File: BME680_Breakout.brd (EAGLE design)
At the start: 160 x 100 mm, 23 parts, among them U1 BME680, U4 PCA9515ADP, U8 LD1117XX

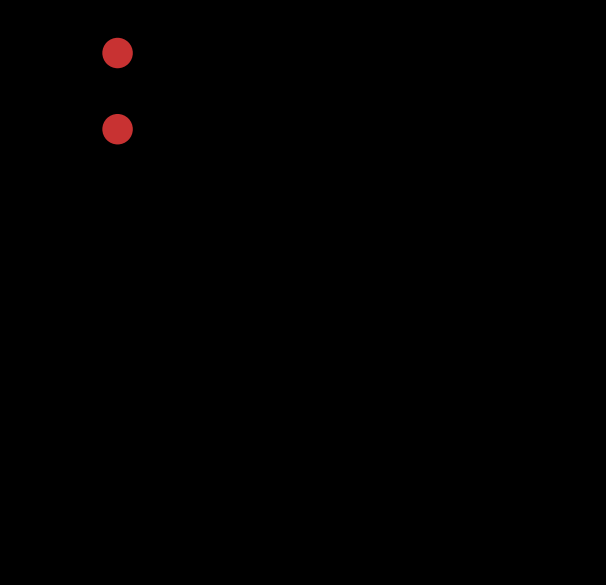
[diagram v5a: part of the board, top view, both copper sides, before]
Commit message: asded zener diode and ptc fuse to address select input
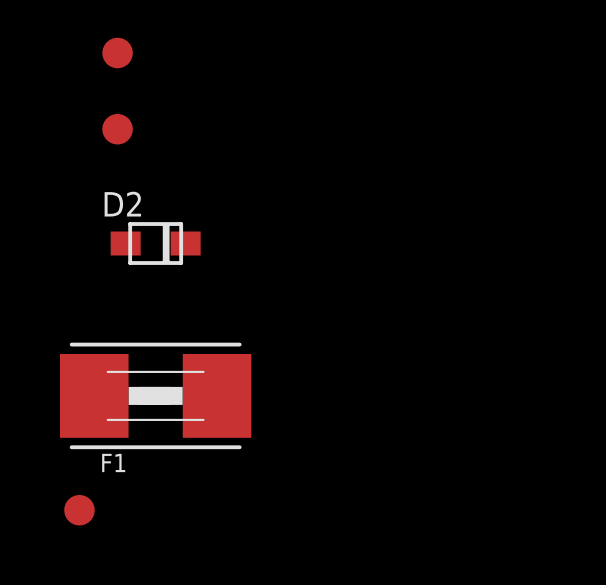
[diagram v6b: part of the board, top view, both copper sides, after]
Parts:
- added D2: DDZ3V3BSF-7, adafruit:SOD-323F
- added F1: (no value), adafruit:1812
- added TP4: TEST-POINT3X4, SparkFun-Passives:PAD.03X.04
- D1: value (none) -> 1N4148
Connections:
- new net ADDR_SELECT_VCCIO: F1.2, JP1.7
- net ADDR_SELECT_3V3: now also D2.C, F1.1, TP4.P$1; no longer JP1.7
- net GND: now also D2.A
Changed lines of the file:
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@@
 <element name="SJ2" library="SparkFun-Passives" package="PAD-JUMPER-2-NO_YES_SILK" value="JUMPER-PAD-2-NOYES_SILK" x="-49.53" y="-25.4"/>
 <element name="R6" library="SparkFun-Passives" package="0805" value="10k" x="-53.34" y="-25.4"/>
-<element name="D1" library="adafruit" package="SOD-323F" value="" x="-52.07" y="-30.48"/>
+<element name="D1" library="adafruit" package="SOD-323F" value="1N4148" x="-52.07" y="-30.48"/>
 <element name="R3" library="SparkFun-Passives" package="0805" value="10k" x="-57.15" y="-29.21"/>
 <element name="U8" library="wicked-device" package="DPAK" value="LD1117XX" x="-53.34" y="-39.37"/>
@@
 <element name="TP2" library="SparkFun-Passives" package="PAD.03X.04" value="TEST-POINT3X4" x="-68.58" y="-48.26"/>
 <element name="TP3" library="SparkFun-Passives" package="PAD.03X.04" value="TEST-POINT3X4" x="-68.58" y="-50.8"/>
+<element name="D2" library="adafruit" package="SOD-323F" value="DDZ3V3BSF-7" x="-67.31" y="-54.61"/>
+<element name="F1" library="adafruit" package="1812" value="" x="-67.31" y="-59.69"/>
+<element name="TP4" library="SparkFun-Passives" package="PAD.03X.04" value="TEST-POINT3X4" x="-69.85" y="-63.5"/>
 </elements>
 <signals>
@@
 <contactref element="C5" pad="2"/>
 <contactref element="R7" pad="2"/>
+<contactref element="D2" pad="A"/>
+<wire x1="-67.68" y1="-41.91" x2="-68.31" y2="-54.61" width="0" layer="19" extent="1-1"/>
 <wire x1="-63.87" y1="-41.91" x2="-67.68" y2="-41.91" width="0" layer="19" extent="1-1"/>
 <wire x1="-60.06" y1="-41.91" x2="-63.87" y2="-41.91" width="0" layer="19" extent="1-1"/>
@@
 <contactref element="SJ2" pad="2"/>
 <contactref element="R3" pad="2"/>
-<contactref element="JP1" pad="7"/>
+<contactref element="F1" pad="1"/>
+<contactref element="D2" pad="C"/>
+<contactref element="TP4" pad="P$1"/>
+<wire x1="-69.356" y1="-59.69" x2="-69.85" y2="-63.5" width="0" layer="19" extent="1-1"/>
+<wire x1="-66.31" y1="-54.61" x2="-69.356" y2="-59.69" width="0" layer="19" extent="1-1"/>
+<wire x1="-56.25" y1="-29.21" x2="-66.31" y2="-54.61" width="0" layer="19" extent="1-1"/>
 <wire x1="-49.08" y1="-25.4" x2="-56.25" y2="-29.21" width="0" layer="19" extent="1-1"/>
-<wire x1="-29.21" y1="-20.32" x2="-49.08" y2="-25.4" width="0" layer="19" extent="1-1"/>
-<wire x1="-16.5275" y1="2.61" x2="-29.21" y2="-20.32" width="0" layer="19" extent="1-1"/>
+<wire x1="-16.5275" y1="2.61" x2="-49.08" y2="-25.4" width="0" layer="19" extent="1-1"/>
 </signal>
 <signal name="SLAVE_SCL_3V3">
@@
 <wire x1="-31.75" y1="-20.32" x2="-51.07" y2="-30.48" width="0" layer="19" extent="1-1"/>
 </signal>
+<signal name="ADDR_SELECT_VCCIO">
+<contactref element="JP1" pad="7"/>
+<contactref element="F1" pad="2"/>
+<wire x1="-29.21" y1="-20.32" x2="-65.264" y2="-59.69" width="0" layer="19" extent="1-1"/>
+</signal>
 </signals>

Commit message: initial routing of PCB
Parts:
- added SJ1: JUMPER-PAD-2-NC_BY_TRACE, SparkFun-Passives:PAD-JUMPER-2-NC_BY_TRACE_YES_SILK
- added SJ3: SOLDERJUMPERNC2, SparkFun-Retired:SJ_2S-NOTRACE
- added STANDOFF1, STANDOFF2, STANDOFF3, STANDOFF4: STAND-OFF, SparkFun-Electromechanical:STAND-OFF
- added U$1: (no value), wicked-device:WICKEDLOGOTYPE2
- added U$2: (no value), wicked-device:WICKEDLOGOTYPE
- moved TP2 109.5 mm to (23.4, 11.2)
- moved R7 107.1 mm to (21.8, 15.5), turned to 270 degrees
- moved C5 106.8 mm to (28.7, 9.65), turned to 270 degrees
- moved TP1 106.6 mm to (23.4, 8.13)
- moved C4 104.5 mm to (31.8, 6.35), turned to 180 degrees
- moved TP4 103.3 mm to (7.62, 4.83)
- moved F1 102.6 mm to (10.2, 7.62)
- moved TP3 102.0 mm to (11.7, 12.2)
- moved U8 101.2 mm to (33.8, 12.2)
- moved D2 99.3 mm to (7.11, 11.2)
- moved R3 82.6 mm to (13.0, 14.5), turned to 180 degrees
- moved R6 77.7 mm to (15.2, 11.2), turned to 270 degrees
- moved D1 77.3 mm to (15.2, 7.62), turned to 270 degrees
- moved SJ5 66.0 mm to (17.3, 6.86), turned to 180 degrees
- moved SJ4 65.7 mm to (20.8, 6.86)
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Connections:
- net SJ_MASTER_SCL_3V3 renamed SJ_MASTER_SCL_VIO
- net SJ_MASTER_SDA_3V3 renamed SJ_MASTER_SDA_VIO
- removed net MASTER_SCL_3V3: SJ5.1
- removed net MASTER_SDA_3V3: SJ4.1
- new net N$1: SJ1.2, U8.4
- net 3.3V: now also SJ1.1, SJ3.2; no longer U8.4
- net MASTER_SCL_VIO: now also JP1.5, SJ5.1; no longer JP1.3
- net MASTER_SDA_VIO: now also SJ4.1
- net SLAVE_I2C_ENABLE: now also JP1.3; no longer JP1.5
- net VCCIO: now also SJ3.1
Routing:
- net 3.3V: track 0.00 -> 71.1 mm, vias 0 -> 4
- net ADDR_SELECT_3V3: track 0.00 -> 32.9 mm
- net GND: track 0.00 -> 27.2 mm, vias 0 -> 9
- net VCCIO: track 0.00 -> 25.1 mm
- net CSB_3V3: track 0.00 -> 23.1 mm
- net SLAVE_I2C_ENABLE: track 0.00 -> 23.1 mm, vias 0 -> 2
- net SJ_MASTER_SCL_VIO: track 0.00 -> 11.3 mm, vias 0 -> 2
- net MASTER_SDA_VIO: track 0.00 -> 10.9 mm
- net MASTER_SCL_VIO: track 0.00 -> 10.9 mm
- net N$1: track 0.00 -> 6.77 mm
- net SLAVE_SDA_3V3: track 0.00 -> 6.47 mm
- net ADDR_SELECT_VCCIO: track 0.00 -> 5.79 mm
- net CSB_VIO: track 0.00 -> 4.59 mm
- net SLAVE_SCL_3V3: track 0.00 -> 3.98 mm
- net SJ_MASTER_SDA_VIO: track 0.00 -> 3.66 mm
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- added copper zone on layer 16, net GND
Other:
- board size 160 x 100 mm -> 38.1 x 25.4 mm
- board text added: "*"
- board text added: "3V"
- board text added: "AD"
- board text added: "CK"
- board text added: "CS"
- board text added: "DT"
- board text added: "EN"
- board text added: "GD"
- board text added: "VI"

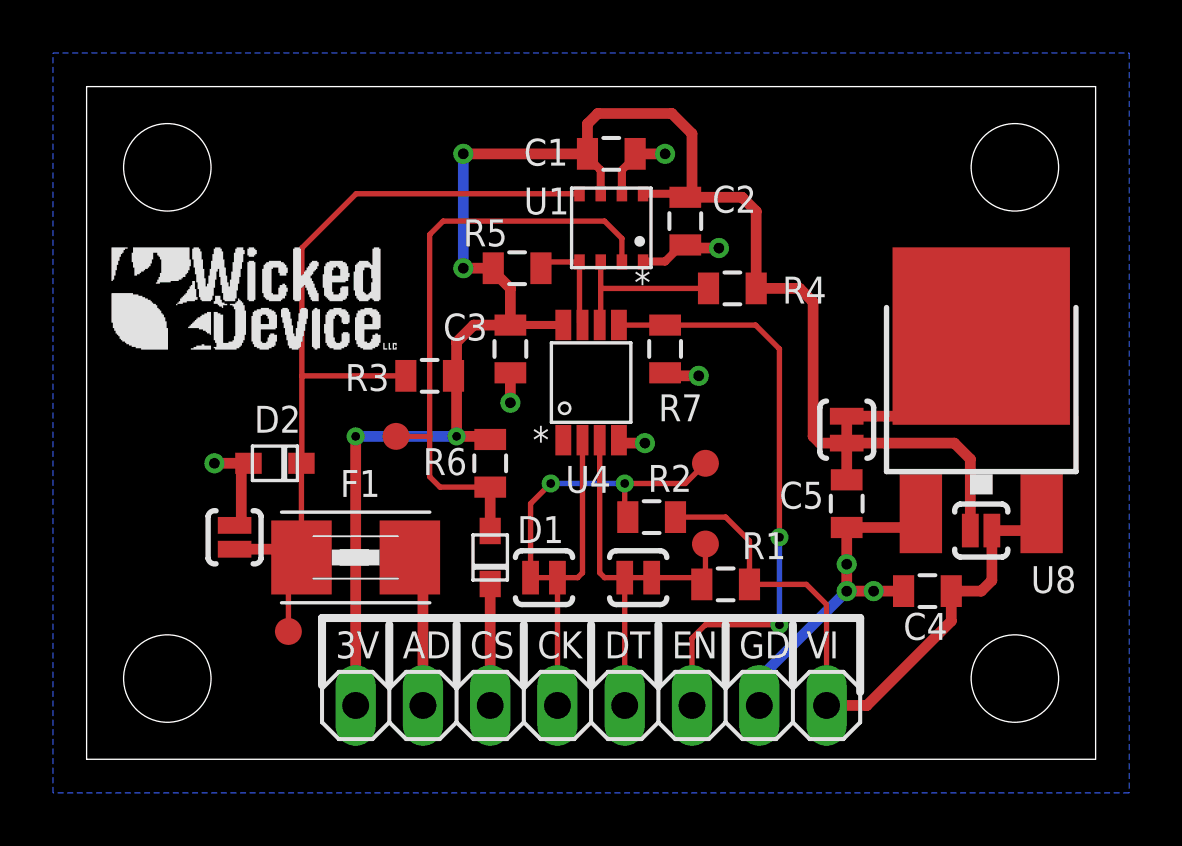
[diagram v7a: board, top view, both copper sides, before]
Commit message: added silk screen to back side; added to solder jumpers; minor routing changes
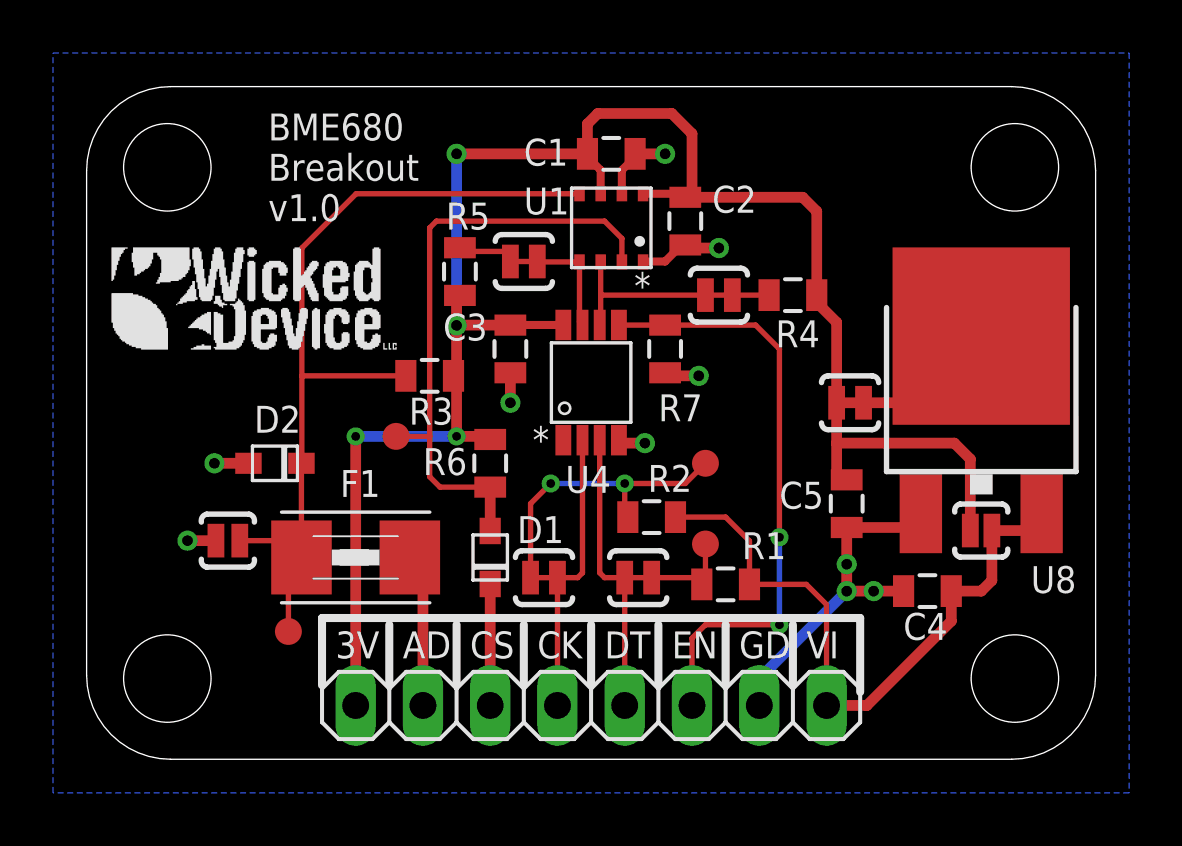
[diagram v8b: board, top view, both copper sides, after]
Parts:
- removed U$2: (no value), wicked-device:WICKEDLOGOTYPE
- added SJ6, SJ7: JUMPER-PAD-2-NC_BY_TRACE, SparkFun-Passives:PAD-JUMPER-2-NC_BY_TRACE_YES_SILK
- moved R4 2.30 mm to (26.7, 17.5)
- moved R5 2.16 mm to (14.1, 18.4), turned to 90 degrees
- moved SJ1 1.02 mm to (28.8, 13.5), turned to 0 degrees
- moved SJ2 0.28 mm to (5.33, 8.26), turned to 0 degrees
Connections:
- new net N$3: R4.2, SJ6.2
- new net N$4: R5.2, SJ7.2
- net SLAVE_SCL_3V3: now also SJ7.1; no longer R5.2
- net SLAVE_SDA_3V3: now also SJ6.1; no longer R4.2
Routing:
- net N$4: track 0.00 -> 2.34 mm
- net GND: track 27.2 -> 25.8 mm, vias 9 -> 10
- net N$3: track 0.00 -> 1.39 mm
- net 3.3V: track 71.1 -> 72.4 mm
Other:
- outline, holes or cut-outs redrawn
- board text added: "3V = 3.3V REG OUT / 3.3V INPUT"
- board text added: "ADDR = AD"
- board text added: "BME680 Breakout v1.0"
- board text added: "FOR I2C BUS ISOLATION"
- board text added: "GD = GROUND"
- board text added: "I2C"
- board text added: "MISO = AD"
- board text added: "MOSI = DT"
- board text added: "NCS = CS"
- board text added: "SCK = CK"
- board text added: "SCL = CK"
- board text added: "SDA = DT"
- board text added: "SELECT = EN"
- board text added: "SPI"
- board text added: "VI = 4.1 - 15V INPUT"
